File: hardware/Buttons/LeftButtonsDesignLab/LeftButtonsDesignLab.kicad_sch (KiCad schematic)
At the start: 5 parts, among them J1 Conn_01x04, J2 Conn_01x01, SW1 SW_Push, SW2 SW_Push, SW3 SW_Push

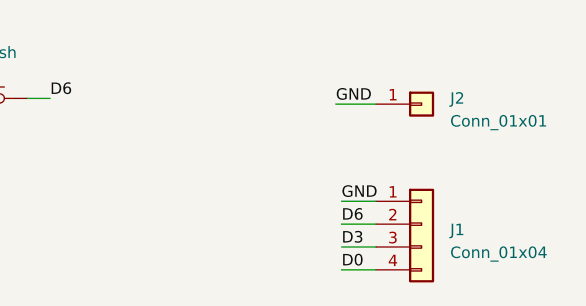
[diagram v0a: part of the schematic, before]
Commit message: BOM of buttons generated
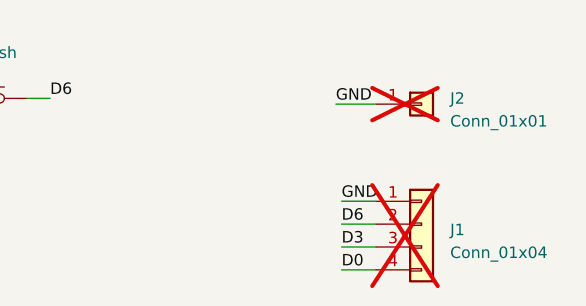
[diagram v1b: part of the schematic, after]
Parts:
- J1, J2: now not fitted
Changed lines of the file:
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@@
   )
   (symbol (lib_id "Connector_Generic:Conn_01x04") (at 163.83 52.07 0) (unit 1)
-    (in_bom yes) (on_board yes) (dnp no) (fields_autoplaced)
+    (in_bom yes) (on_board yes) (dnp yes) (fields_autoplaced)
     (property "Reference" "J1" (at 167.005 52.705 0)
       (effects (font (size 1.27 1.27)) (justify left))
@@
   )
   (symbol (lib_id "Connector_Generic:Conn_01x01") (at 163.83 38.735 0) (unit 1)
-    (in_bom yes) (on_board yes) (dnp no) (fields_autoplaced)
+    (in_bom yes) (on_board yes) (dnp yes) (fields_autoplaced)
     (property "Reference" "J2" (at 167.005 38.1 0)
       (effects (font (size 1.27 1.27)) (justify left))

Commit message: Update all PCB and schematics
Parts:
- removed J2: Conn_01x01, Connector_PinHeader_2.54mm:PinHeader_1x01_P2.54mm_Vertical, symbol Connector_Generic:Conn_01x01
- J1: footprint Connector_PinHeader_2.54mm:PinHeader_1x04_P2.54mm_Vertical -> Design:JST_S4B-PH-K-S_LF__SN_; LCSC# (none) -> C157926; now fitted
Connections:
- net D0: now also J1.1 (Pin_1); no longer J1.4 (Pin_4)
- net D3: now also J1.2 (Pin_2); no longer J1.3 (Pin_3)
- net D6: now also J1.3 (Pin_3); no longer J1.2 (Pin_2)
- net GND: now also J1.4 (Pin_4); no longer J1.1 (Pin_1)
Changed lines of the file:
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@@
-    (stroke (width 0) (type default))
-  )
-  (wire (pts (xy 154.305 38.735) (xy 158.75 38.735))
     (stroke (width 0) (type default))
   )
@@
   )
   (label "GND" (at 154.94 49.53 0) (fields_autoplaced)
-    (effects (font (size 1.27 1.27)) (justify left bottom))
-  )
-  (label "GND" (at 154.305 38.735 0) (fields_autoplaced)
     (effects (font (size 1.27 1.27)) (justify left bottom))
   )
@@
     )
   )
-  (symbol (lib_id "Connector_Generic:Conn_01x04") (at 163.83 52.07 0) (unit 1)
-    (in_bom yes) (on_board yes) (dnp yes) (fields_autoplaced)
-    (property "Reference" "J1" (at 167.005 52.705 0)
-      (effects (font (size 1.27 1.27)) (justify left))
+  (symbol (lib_id "Connector_Generic:Conn_01x04") (at 163.83 54.61 0) (mirror x) (unit 1)
+    (in_bom yes) (on_board yes) (dnp no)
+    (property "Reference" "J1" (at 163.83 44.45 0)
+      (effects (font (size 1.27 1.27)))
     )
-    (property "Value" "Conn_01x04" (at 167.005 55.245 0)
-      (effects (font (size 1.27 1.27)) (justify left))
+    (property "Value" "Conn_01x04" (at 163.83 46.99 0)
+      (effects (font (size 1.27 1.27)))
     )
-    (property "Footprint" "Connector_PinHeader_2.54mm:PinHeader_1x04_P2.54mm_Vertical" (at 163.83 52.07 0)
+    (property "Footprint" "Design:JST_S4B-PH-K-S_LF__SN_" (at 163.83 54.61 0)
       (effects (font (size 1.27 1.27)) hide)
     )
-    (property "Datasheet" "~" (at 163.83 52.07 0)
+    (property "Datasheet" "https://datasheet.lcsc.com/lcsc/2304140030_JST-S4B-PH-K-S-LF-SN_C157926.pdf" (at 163.83 54.61 0)
+      (effects (font (size 1.27 1.27)) hide)
+    )
+    (property "LCSC#" "C157926" (at 163.83 54.61 0)
       (effects (font (size 1.27 1.27)) hide)
     )
@@
         )
       )
-    )
-  )
-  (symbol (lib_id "Connector_Generic:Conn_01x01") (at 163.83 38.735 0) (unit 1)
-    (in_bom yes) (on_board yes) (dnp yes) (fields_autoplaced)
-    (property "Reference" "J2" (at 167.005 38.1 0)
-      (effects (font (size 1.27 1.27)) (justify left))
-    )
-    (property "Value" "Conn_01x01" (at 167.005 40.64 0)
-      (effects (font (size 1.27 1.27)) (justify left))
-    )
-    (property "Footprint" "Connector_PinHeader_2.54mm:PinHeader_1x01_P2.54mm_Vertical" (at 163.83 38.735 0)
-      (effects (font (size 1.27 1.27)) hide)
-    )
-    (property "Datasheet" "~" (at 163.83 38.735 0)
-      (effects (font (size 1.27 1.27)) hide)
-    )
-    (pin "1")
-    (instances
-      (project "LeftButtonsDesignLab"
-        (path "/cb01e4f9-1b61-4764-a526-4852e06b6614"
-          (reference "J2") (unit 1)
-        )
-      )
-      (project "ButtonDesignLab"
-        (path "/e63e39d7-6ac0-4ffd-8aa3-1841a4541b55"
-          (reference "J7") (unit 1)
-        )
-      )
